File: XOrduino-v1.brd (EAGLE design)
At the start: 68.6 x 53.3 mm, 56 parts, among them J1 USB MICRO, J2 8x1F-H8.5, J3 8x1F-H8.5, J4 6x1F-H8.5, U1 ATMEGA32U4-XUAU, U10 SLIDER, U3 2.5mm, U4 2.5mm, U5 2.5mm, U6 2.5mm, U7 TEMT6000, U8 LMV358, U9 MIC9.7MM, X1 USBPCB, X2 USB-MB-H, Y1 16MHz

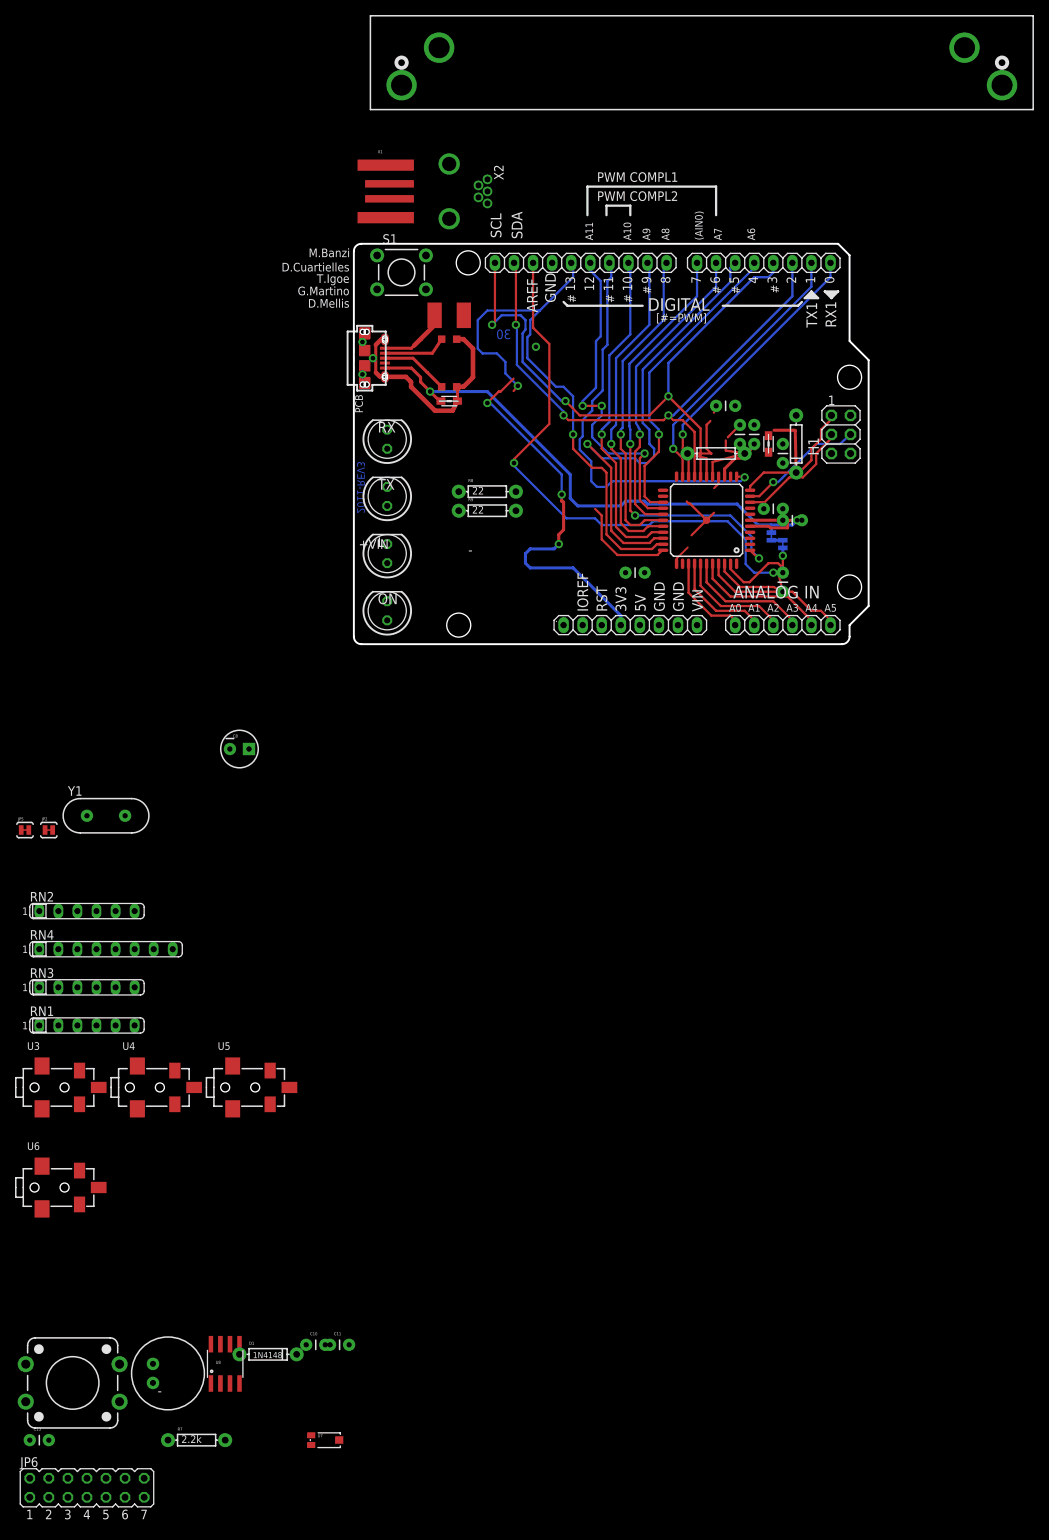
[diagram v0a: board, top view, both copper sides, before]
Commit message: Attempt to route the board.  90% routed; may need to go to 4 layer board.
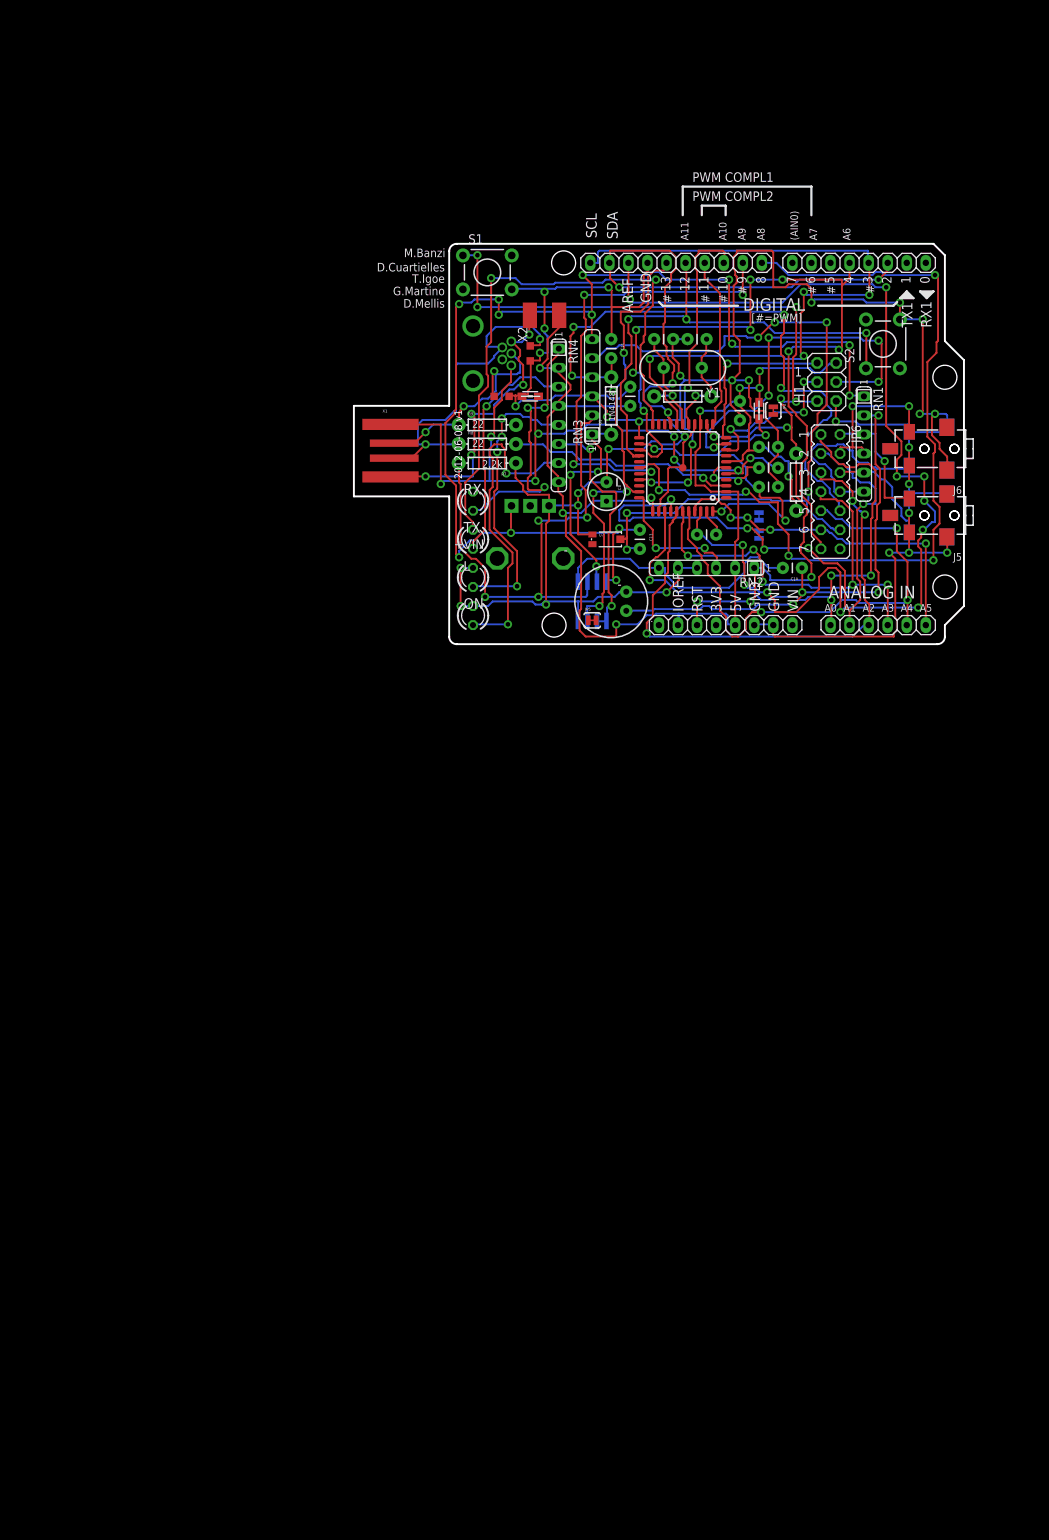
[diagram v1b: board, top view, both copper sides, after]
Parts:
- removed JP1: 10x1F-H8.5, SmartPrj:1X10
- removed U3, U4, U5, U6: 2.5mm, SparkFun:STEREOJACK2.5MM_SMD
- added J5, J6, J7, J8: 2.5mm, SparkFun:STEREOJACK2.5MM_SMD
- J1: value USB MICRO -> 10x1F-H8.5; device SmartPrj:CON2_USB_MICRO_B_AT -> SmartPrj:1X10
- JP6: value (none) -> Sensor Routing
- L, ON, RX, TX: device led:LED5MM -> led:LED3MM
- S1: value (none) -> RESET
- S2: value 12mm Button -> 6mm Button; device SparkFun:TACTILE-PTH-12MM -> SparkFun-Electromechanical:TACTILE-PTH
- U10: value SLIDER -> 10k; device SparkFun:SLIDER -> SparkFun-Electromechanical:ALPS_POT
- moved S2 175.5 mm to (70.5, 40.0), turned to 90 degrees
- moved JP6 165.6 mm to (63.5, 20.3), turned to 270 degrees
- moved C13 146.0 mm to (38.1, 15.2), turned to 270 degrees
- moved C11 139.1 mm to (34.3, 40.6), turned to 270 degrees
- moved R7 135.8 mm to (17.8, 24.1), turned to 180 degrees
- moved D1 134.4 mm to (34.3, 31.8), turned to 90 degrees
- moved RN1 129.3 mm to (67.9, 26.7), turned to 270 degrees
- moved U7 125.7 mm to (33.7, 14.0)
- moved C10 122.8 mm to (59.7, 10.2), turned to 180 degrees
- moved U9 118.6 mm to (34.3, 5.71), turned to 180 degrees
- moved U8 112.8 mm to (31.8, 5.71), flipped to the bottom
- moved JP2 111.5 mm to (55.9, 31.1), turned to 270 degrees
- moved RN3 104.6 mm to (31.8, 34.3), turned to 90 degrees
- moved Y1 97.3 mm to (43.8, 36.8), turned to 180 degrees
- moved RN2 94.4 mm to (47.0, 10.2), turned to 180 degrees
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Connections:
- removed net USBID: J1.P4
- net +5V: now also RN4.8; no longer RN4.6
- net 5V: now also U10.P$3; no longer U10.3
- net A0: now also JP6.1; no longer JP6.2
- net A1: now also JP6.3; no longer JP6.4
- net A2: now also JP6.5; no longer JP6.6
- net A3: now also JP6.7; no longer JP6.8
- net A4: now also JP6.9; no longer JP6.10
- net A5: now also JP6.11; no longer JP6.12
- net AREF: now also J1.8; no longer JP1.8
- net D+: no longer J1.P3
- net D-: no longer J1.P2
- net D2/SDA: now also J1.9; no longer JP1.9
- net D3/SCL: now also J1.10; no longer JP1.10
- net D4: now also JP6.13; no longer JP6.14
- net GND: now also J1.7, J5.1, J5.5, J6.1, J6.5, J7.1, J7.5, J8.1, J8.5, S2.4, U10.P$1; no longer J1.S1, J1.S2, J1.S3, J1.S4, J1.S5, J1.S6, JP1.7, S1.3, S2.3, U10.1, U3.1, U3.5, U4.1, U4.5, U5.1, U5.5, U6.1, U6.5
- net IO10*: now also J1.3; no longer JP1.3
- net IO11*: now also J1.4; no longer JP1.4
- net IO12: now also J1.5; no longer JP1.5
- net IO13*: now also J1.6; no longer JP1.6
- net IO8: now also J1.1; no longer JP1.1
- net IO9*: now also J1.2; no longer JP1.2
- net LIGHT: now also JP6.12; no longer JP6.11
- net N$1: now also RN4.3; no longer RN4.1
- net N$2: now also RN4.5; no longer RN4.7
- net N$3: now also RN4.7; no longer RN4.5
- net N$4: now also RN4.1; no longer RN4.3
- net N$6: now also RN4.6; no longer RN4.8
- net RA: now also J5.4, JP6.2; no longer JP6.1, U3.4
- net RB: now also J6.4, JP6.4; no longer JP6.3, U4.4
- net RC: now also J7.4, JP6.6; no longer JP6.5, U5.4
- net RD: now also J8.4, JP6.8; no longer JP6.7, U6.4
- net RESET: no longer S1.2
- net SLIDER: now also JP6.14, U10.P$2; no longer JP6.13, U10.2A
- net SOUND: now also JP6.10; no longer JP6.9
- net UGND: no longer J1.P5
- net XUSB: no longer J1.P1
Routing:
- net GND: track 41.7 -> 409.7 mm, vias 4 -> 30
- net +5V: track 18.5 -> 185.0 mm, vias 0 -> 9
- net 5V: track 0.00 -> 157.2 mm, vias 0 -> 13
- net RESET: track 0.00 -> 132.3 mm, vias 0 -> 10
- net LIGHT: track 0.00 -> 98.9 mm, vias 0 -> 6
- net SOUND: track 0.00 -> 79.9 mm, vias 0 -> 4
- net TXLED: track 0.00 -> 78.9 mm, vias 0 -> 2
- net IO8: track 42.6 -> 114.0 mm, vias 1 -> 5
- net N$5: track 0.00 -> 67.5 mm, vias 0 -> 4
- net A1: track 13.7 -> 80.6 mm, vias 0 -> 5
- net D4: track 41.0 -> 105.9 mm, vias 1 -> 8
- net N$9: track 0.00 -> 64.9 mm, vias 0 -> 4
- net D5*: track 62.5 -> 0.00 mm, vias 1 -> 0
- net A0: track 12.2 -> 72.8 mm, vias 0 -> 4
- net D7: track 59.3 -> 0.00 mm, vias 3 -> 0
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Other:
- board size 68.6 x 53.3 mm -> 81.3 x 53.3 mm
- board text added: "2012-06-08 v1"
- board text removed: "2011-REV3"
- board text removed: "30"

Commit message: First full layout for XOrduino. (v1)
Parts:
- moved JP5 4.02 mm to (35.6, 1.91), flipped to the bottom
- moved JP3 3.81 mm to (50.2, 14.6), flipped to the top, turned to 0 degrees
- moved JP4 1.42 mm to (52.7, 16.4), flipped to the top
- moved R7 0.63 mm to (17.8, 23.5)
- moved R9 0.63 mm to (17.8, 29.8)
- moved S1 0.63 mm to (17.8, 48.9)
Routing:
- net AREF: track 140.3 -> 43.6 mm, vias 11 -> 0
- net IO8: track 114.0 -> 41.5 mm, vias 5 -> 1
- net GND: track 409.7 -> 344.1 mm, vias 30 -> 3
- net RXLED: track 0.00 -> 64.2 mm, vias 0 -> 3
- net SLIDER: track 0.00 -> 59.1 mm
- net 5V: track 157.2 -> 99.5 mm, vias 13 -> 2
- net D0/RX: track 0.00 -> 55.0 mm, vias 0 -> 2
- net D1/TX: track 0.00 -> 52.1 mm, vias 0 -> 2
- net D7: track 0.00 -> 50.9 mm, vias 0 -> 2
- net D5*: track 0.00 -> 50.5 mm, vias 0 -> 2
- net AVCC: track 47.9 -> 95.1 mm
- net D6*: track 0.00 -> 46.1 mm, vias 0 -> 2
- net TXLED: track 78.9 -> 35.7 mm, vias 2 -> 1
- net LIGHT: track 98.9 -> 61.6 mm, vias 6 -> 0
- net RD+: track 0.00 -> 34.4 mm, vias 0 -> 2
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- added copper zone on layer 1, net +5V
- added copper zone on layer 16, net GND
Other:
- board text added: "C. Scott Ananian"
- board text removed: "ITALY"
- board text removed: "MADE IN"

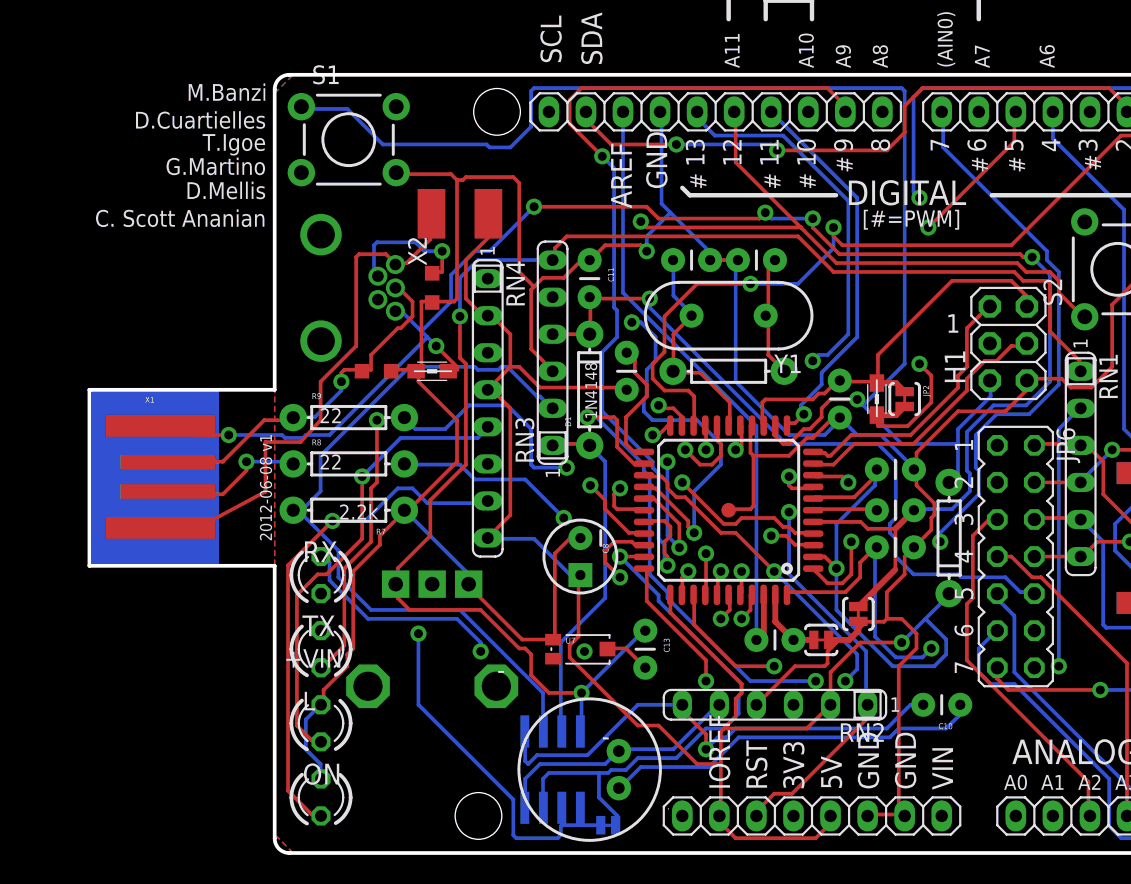
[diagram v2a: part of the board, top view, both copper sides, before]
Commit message: XOrduino v2 -- move USB plug up a bit to allow XOstick to fit underneath.
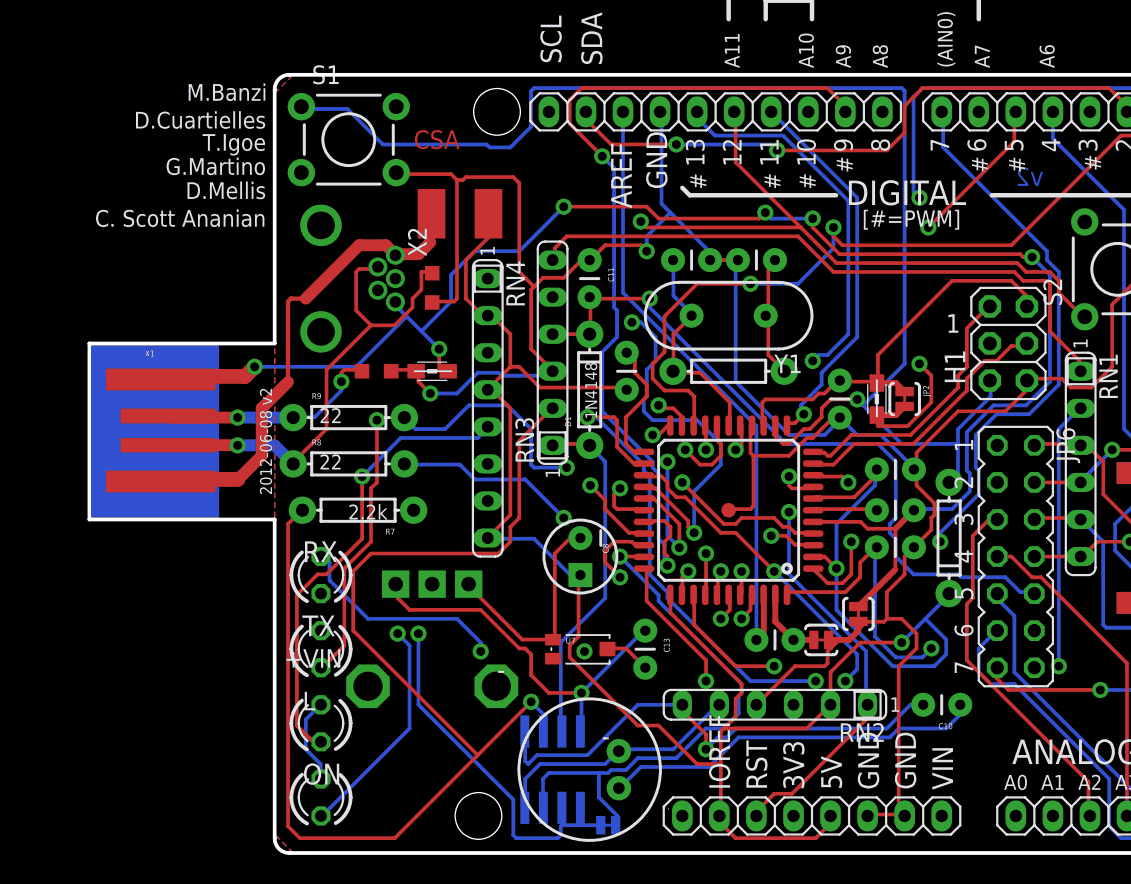
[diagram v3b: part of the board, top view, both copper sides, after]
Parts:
- moved X1 3.18 mm to (5.08, 29.0)
- moved R7 0.63 mm to (18.4, 23.5)
- moved X2 0.63 mm to (15.9, 39.4)
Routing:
- net N$5: track 50.8 -> 83.5 mm, vias 0 -> 1
- net GND: track 344.1 -> 314.3 mm, vias 3 -> 4
- net N$3: track 34.9 -> 27.1 mm
- net 5V: track 99.5 -> 96.5 mm, vias 2 -> 1
- net UGND: track 115.4 -> 112.4 mm
- net XUSB: track 35.8 -> 33.0 mm
- net D-: track 34.7 -> 33.4 mm, vias 2 -> 1
- net D+: track 25.0 -> 26.2 mm, vias 1 -> 2
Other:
- outline, holes or cut-outs redrawn
- board text added: "2012-06-08 v2"
- board text added: "CSA"
- board text added: "v2"
- board text removed: "2012-06-08 v1"
